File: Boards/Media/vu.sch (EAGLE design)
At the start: 53 parts, among them IC1 LM3914N, IC2 LM324D, IC3 LM3914N, IC4 LM3914N, IC5 LM3914N

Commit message: Lots of prgress on media related boards.
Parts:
- R1, R10, R11, R12, R13, R14, R15, R16, R2, R3, R4, R5, R6, R7, R8, R9: device 1_SparkFun-Resistors:RESISTOR1206 -> 1_SparkFun-Resistors:RESISTOR0603
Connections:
- net CH1: now also R7.2; no longer C10.1, C13.1, C2.1, R13.2
- net CH2: now also C13.1, R6.2; no longer R14.2
- net CH3: now also C2.1, R12.1; no longer R15.1
- net CH4: now also C10.1, R1.1; no longer R16.1
- net GND: now also R13.1, R14.1, R15.1, R16.1; no longer R10.1, R11.1, R12.1, R9.1
- net N$1: now also R11.2; no longer R6.2
- net N$10: now also R13.2, R3.1; no longer R12.2, R7.1
- net N$11: now also R10.1, R12.2; no longer R15.2, R5.1
- net N$12: now also R11.1, R16.2; no longer R11.2, R6.1
- net N$13: now also R7.1, R8.2; no longer R13.1, R3.2
- net N$14: now also R15.2, R9.2; no longer R10.2, R4.2
- net N$15: now also R5.1; no longer R2.1
- net N$16: now also R4.2, R6.1; no longer R1.2, R14.1
- net N$2: now also R9.1; no longer R4.1
- net N$3: now also R8.1; no longer R3.1
- net N$4: now also R10.2; no longer R5.2
- net N$5: now also R14.2, R5.2; no longer R2.2, R9.2
- net N$6: now also R4.1; no longer R1.1
- net N$7: now also R2.2; no longer R8.2
- net N$8: now also R3.2; no longer R7.2
- net N$9: now also R1.2, R2.1; no longer R16.2, R8.1
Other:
- moved on the sheet: R1, R10, R11, R12, R13, R14, R15, R16, R2, R3, R4, R5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

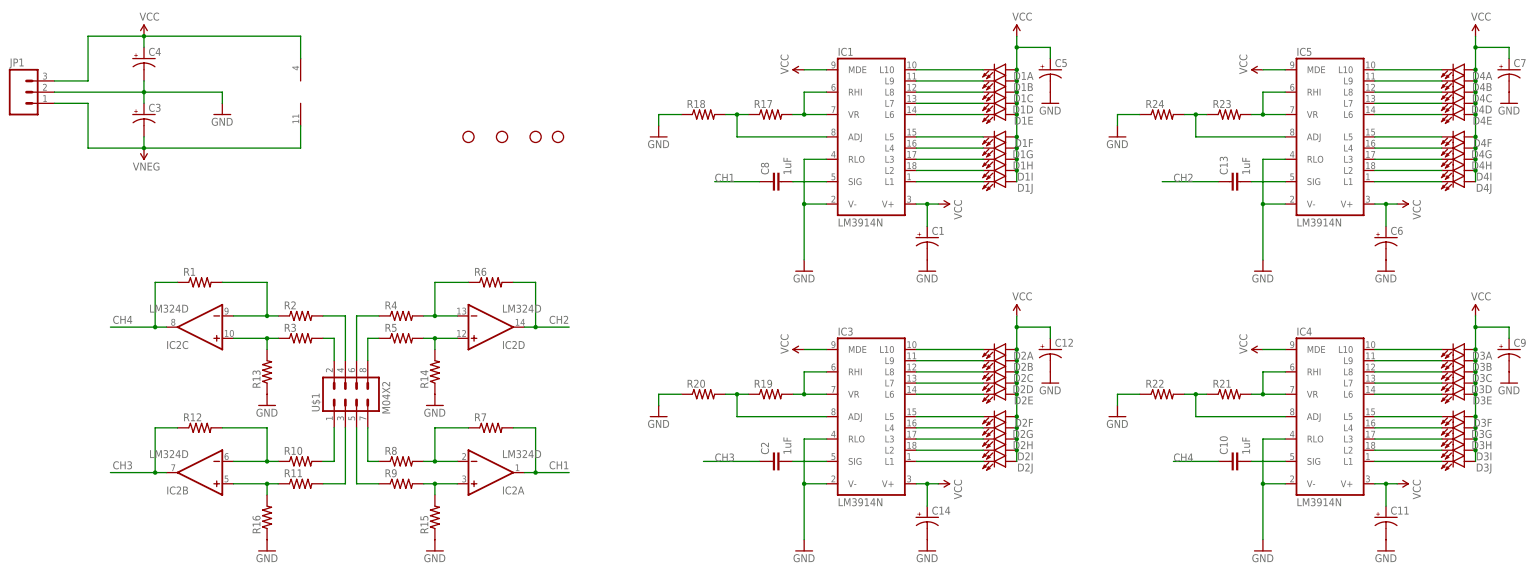
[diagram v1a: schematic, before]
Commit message: Final gerbers and board updates! Fixed PCB violations, now passes FreeDFM check!
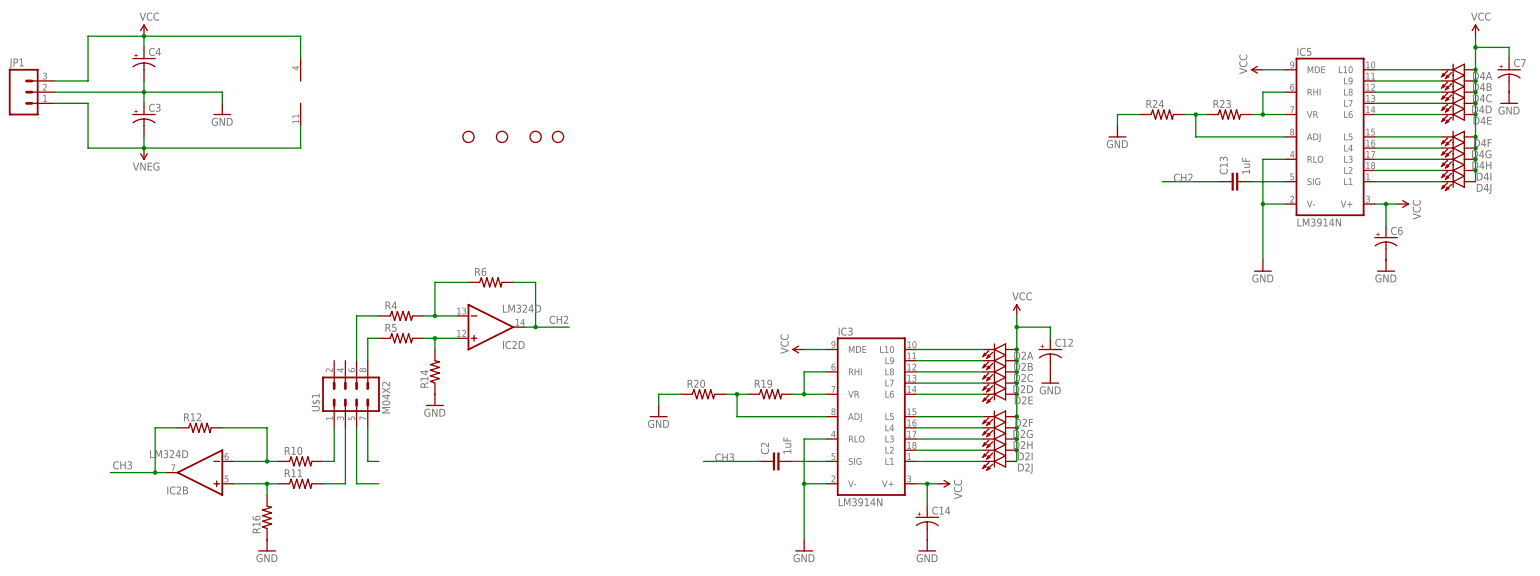
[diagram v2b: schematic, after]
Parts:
- removed C1, C11, C5, C9: (no value), 1_SparkFun-Capacitors:CAP_POL1206
- removed C10, C8: 1uF, 1_SparkFun-Capacitors:CAP1206
- removed D1, D3: (no value), 1_SparkFun-LED:LED_BARGRAPH_10
- removed IC1, IC4: LM3914N, linear:LM3914N
- removed R1, R13, R15, R2, R3, R7, R8, R9: (no value), 1_SparkFun-Resistors:RESISTOR0603
- removed R17, R18, R21, R22: (no value), 1_SparkFun-Resistors:RESISTOR1206
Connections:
- removed net CH1: C8.1, IC2A.OUT, R7.2
- removed net CH4: C10.1, IC2C.OUT, R1.1
- removed net N$10: IC2C.+IN, R13.2, R3.1
- removed net N$13: IC2A.-IN, R7.1, R8.2
- removed net N$14: IC2A.+IN, R15.2, R9.2
- removed net N$17: D1B.C, IC1.L9
- removed net N$18: D1C.C, IC1.L8
- removed net N$19: D1D.C, IC1.L7
- removed net N$20: D1E.C, IC1.L6
- removed net N$21: D1F.C, IC1.L5
- removed net N$22: D1G.C, IC1.L4
- removed net N$23: D1H.C, IC1.L3
- removed net N$24: D1I.C, IC1.L2
- removed net N$25: D1J.C, IC1.L1
- removed net N$26: D1A.C, IC1.L10
- removed net N$27: C8.2, IC1.SIG
- removed net N$28: IC1.ADJ, R17.1, R18.2
- removed net N$29: IC1.RHI, IC1.VR, R17.2
- removed net N$43: D3B.C, IC4.L9
- removed net N$44: D3C.C, IC4.L8
- removed net N$45: D3D.C, IC4.L7
- removed net N$46: D3E.C, IC4.L6
- removed net N$47: D3F.C, IC4.L5
- removed net N$48: D3G.C, IC4.L4
- removed net N$49: D3H.C, IC4.L3
- removed net N$50: D3I.C, IC4.L2
- removed net N$51: D3J.C, IC4.L1
- removed net N$52: D3A.C, IC4.L10
- removed net N$53: C10.2, IC4.SIG
- removed net N$54: IC4.RHI, IC4.VR, R21.2
- removed net N$55: IC4.ADJ, R21.1, R22.2
- removed net N$7: R2.2, U$1.4
- removed net N$8: R3.2, U$1.2
- removed net N$9: IC2C.-IN, R1.2, R2.1
- net GND: no longer C1.-, C11.-, C5.-, C9.-, IC1.RLO, IC1.V-, IC4.RLO, IC4.V-, R13.1, R15.1, R18.1, R22.1
- net N$2: no longer R9.1
- net N$3: no longer R8.1
- net VCC: no longer C1.+, C11.+, C5.+, C9.+, D1A.A, D1B.A, D1C.A, D1D.A, D1E.A, D1F.A, D1G.A, D1H.A, D1I.A, D1J.A, D3A.A, D3B.A, D3C.A, D3D.A, D3E.A, D3F.A, D3G.A, D3H.A, D3I.A, D3J.A, IC1.MDE, IC1.V+, IC4.MDE, IC4.V+
